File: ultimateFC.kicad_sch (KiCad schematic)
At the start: 73 parts, among them J1 USB_B_Micro, U14 TPS62824ADMQ, U32 LMR33630CQRNX, U33 STM32H735VGH6, U36 ICM-20602, U37 S25FL064L, U39 BMP280, Y1 CSTNE8M00G550000R0

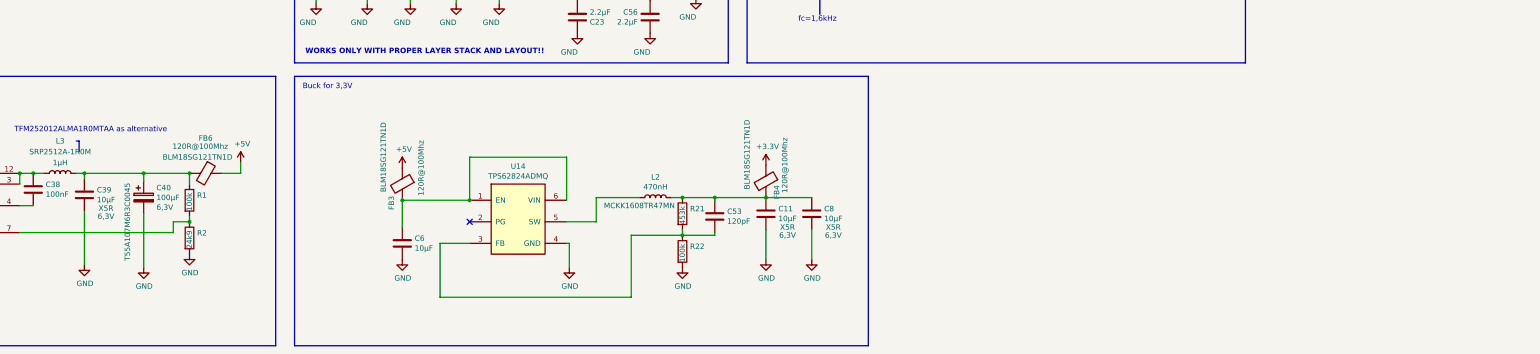
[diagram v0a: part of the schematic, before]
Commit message: add HD DCDC
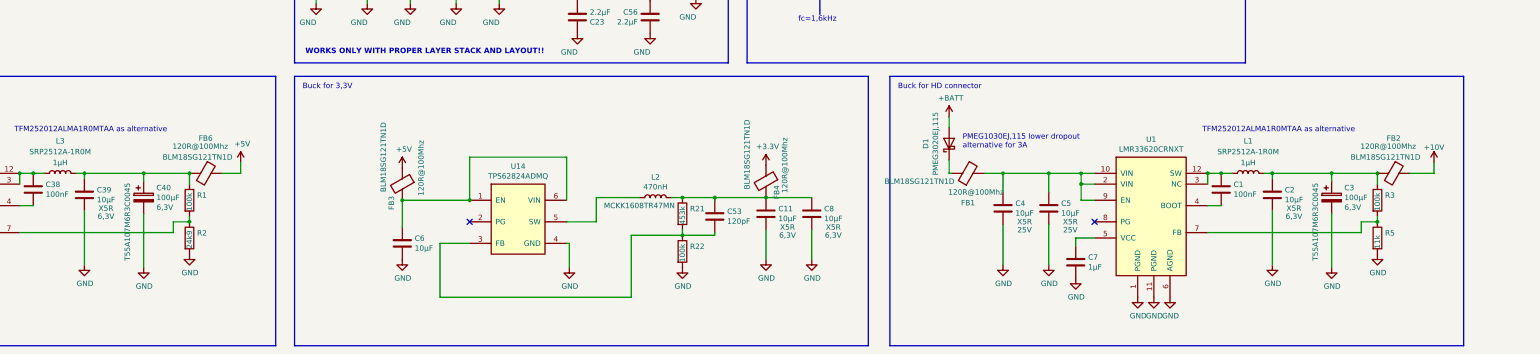
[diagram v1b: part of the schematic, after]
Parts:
- added C1: 100nF, ultimateFC:C_0201_0603Metric_mod, symbol Device:C
- added C2: 10µF, Capacitor_SMD:C_0603_1608Metric, symbol Device:C
- added C3: 100µF, Capacitor_Tantalum_SMD:CP_EIA-3216-10_Kemet-I, symbol ultimateFC-rescue:CP-Device
- added C4, C5: 10µF, Capacitor_SMD:C_1206_3216Metric, symbol Device:C
- added C7: 1µF, Capacitor_SMD:C_0402_1005Metric, symbol Device:C
- added D1: PMEG3020EJ,115, Diode_SMD:D_SOD-323, symbol Device:D_Schottky
- added FB1, FB2: 120R@100Mhz, Inductor_SMD:L_0603_1608Metric, symbol ultimateFC-rescue:Ferrite_Bead-Device
- added L1: 1µH, Inductor_SMD:L_Wuerth_MAPI-2506, symbol Device:L
- added R3: 100k, ultimateFC:R_0201_0603Metric_mod, symbol Device:R
- added R5: 11k, ultimateFC:R_0201_0603Metric_mod, symbol Device:R
- added U1: LMR33620CRNXT, ultimateFC:Texas_RNX0012B, symbol ultimateFC-rescue:LMR33630CQRNX-lib_ultimateFC
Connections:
- net +BATT: now also D1.2 (A)
- net GND: now also C2.2, C3.2, C4.2, C5.2, C7.2, R5.2, U1.1 (PGND), U1.11 (PGND), U1.6 (AGND)
- new net: C4.1, C5.1, FB1.2, U1.10 (VIN), U1.2 (VIN), U1.9 (EN)
- new net: C1.1, L1.1, U1.12 (SW), U1.3 (NC)
- new net: C1.2, U1.4 (BOOT)
- new net: D1.1 (K), FB1.1
- new net: C2.1, C3.1, FB2.2, L1.2, R3.1
- new net: R3.2, R5.1, U1.7 (FB)
- new net: C7.1, U1.5 (VCC)
- new net +10V: FB2.1
- no-connect marks 5 -> 6
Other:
- note added: "Buck for HD connector"

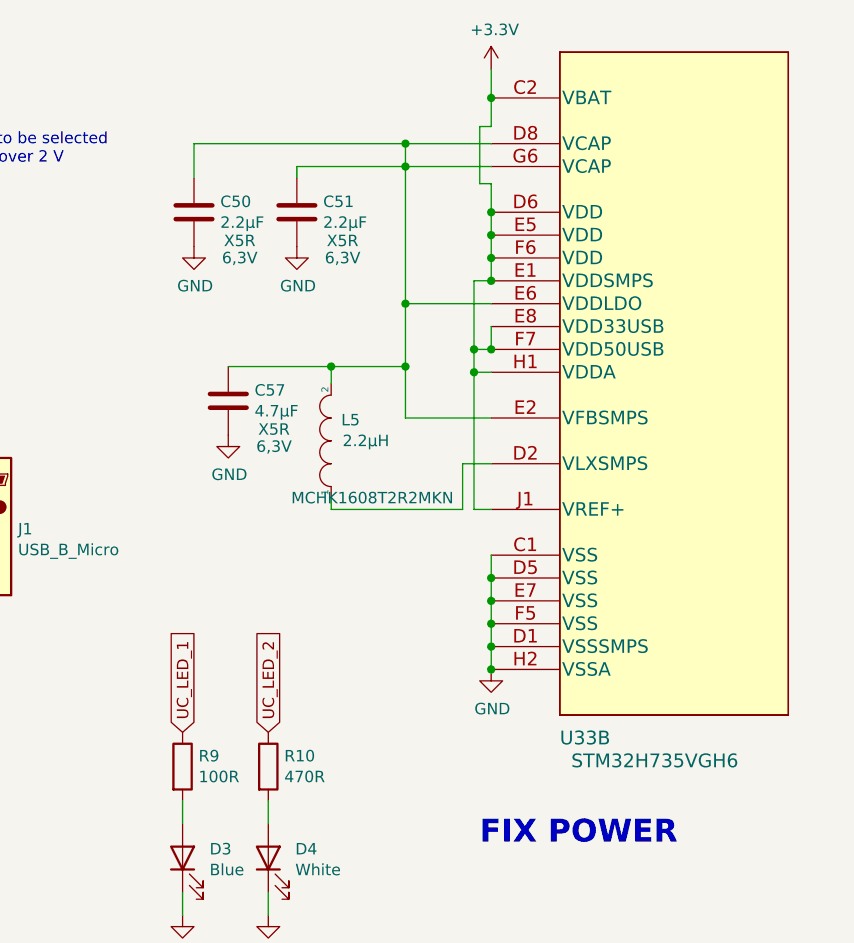
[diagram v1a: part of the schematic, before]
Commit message: update H7 Power symbol (!)
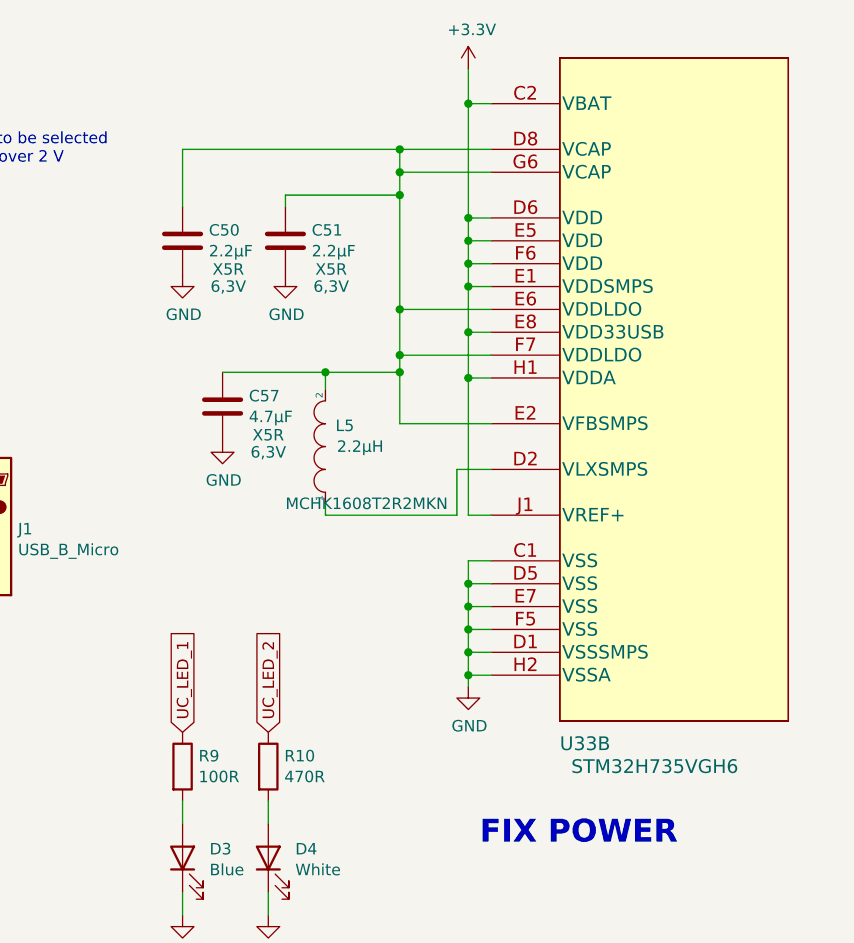
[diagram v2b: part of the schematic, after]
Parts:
- U33: footprint Package_BGA:TFBGA-100_8x8mm_Layout10x10_P0.8mm -> TFBGA100_8X8_STM
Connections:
- net +3V3: no longer U33.F7 (VDD50USB)
- net at C50.1, C51.1, C57.1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: now also U33.F7 (VDDLDO)
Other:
- moved on the sheet: C50, C51, C57, L5, U33B

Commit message: added PADs.... lots of PADs
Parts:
- removed C2: 10µF, Capacitor_SMD:C_0603_1608Metric, symbol Device:C
- removed C22, C23, C24, C25: 2.2µF, Capacitor_SMD:C_0603_1608Metric, symbol Device:C
- removed C27: 10µF, Capacitor_Tantalum_SMD:CP_EIA-3216-18_Kemet-A, symbol ultimateFC-rescue:CP-Device
- removed D1: PMEG3020EJ,115, Diode_SMD:D_SOD-323, symbol Device:D_Schottky
- added C31: 10µF, Capacitor_SMD:C_1206_3216Metric, symbol Device:C
- added C33: 100µF, Capacitor_Tantalum_SMD:CP_EIA-3528-12_Kemet-T, symbol ultimateFC-rescue:CP-Device
- added C34: 4.7µF, Capacitor_SMD:C_0402_1005Metric, symbol Device:C
- added R12, R13, R14, R15, R16, R17, R18, R19, R20, R21, R23: 100R, ultimateFC:R_0201_0603Metric_mod, symbol Device:R
- added TP1, TP10, TP100, TP101, TP102, TP103, TP104, TP105, TP106, TP107, TP108, TP109, TP11, TP110, TP12, TP13, TP14, TP15, TP16, TP17, TP18, TP19, TP2, TP22, TP23, TP24, TP25, TP26, TP27, TP29, TP3, TP30, TP31, TP32, TP33, TP34, TP35, TP36, TP37, TP38, TP39, TP4, TP40, TP41, TP42, TP43, TP44, TP45, TP46, TP47, TP48, TP49, TP5, TP50, TP51, TP52, TP53, TP54, TP55, TP56, TP57, TP58, TP59, TP6, TP60, TP61, TP62, TP63, TP64, TP65, TP66, TP67, TP68, TP69, TP7, TP70, TP71, TP72, TP73, TP74, TP75, TP76, TP77, TP78, TP79, TP8, TP80, TP81, TP82, TP83, TP84, TP85, TP86, TP87, TP88, TP89, TP9, TP90, TP91, TP92, TP93, TP94, TP95, TP96, TP97, TP98, TP99: Pad, TestPoint:TestPoint_Pad_1.5x1.5mm, symbol Connector:TestPoint_Flag
- added TP20, TP21: Pad, TestPoint:TestPoint_Pad_3.0x3.0mm, symbol Connector:TestPoint_Flag
- added U6: BMI270, Package_LGA:Bosch_LGA-14_3x2.5mm_P0.5mm, symbol Sensor_Motion:BMI160
- C10: renamed from C15; value 2.2µF -> 4.7µF; footprint ultimateFC:C_AVX_Super_Low_ESL -> Capacitor_SMD:C_0402_1005Metric
- C12: renamed from C20; value 1µF -> 4.7µF; footprint ultimateFC:C_AVX_Super_Low_ESL -> Capacitor_SMD:C_0402_1005Metric
- C13: renamed from C21; value 2.2µF -> 4.7µF; footprint ultimateFC:C_AVX_Super_Low_ESL -> Capacitor_SMD:C_0402_1005Metric
- C14: renamed from C41; value 1µF -> 4.7µF; footprint ultimateFC:C_AVX_Super_Low_ESL -> Capacitor_SMD:C_0402_1005Metric
- C15: renamed from C42; value 2.2µF -> 4.7µF; footprint ultimateFC:C_AVX_Super_Low_ESL -> Capacitor_SMD:C_0402_1005Metric
- C16: renamed from C43; value 1µF -> 4.7µF; footprint ultimateFC:C_AVX_Super_Low_ESL -> Capacitor_SMD:C_0402_1005Metric
- C17: renamed from C44; value 2.2µF -> 4.7µF; footprint ultimateFC:C_AVX_Super_Low_ESL -> Capacitor_SMD:C_0402_1005Metric
- C29: renamed from C7; footprint Capacitor_SMD:C_0402_1005Metric -> ultimateFC:C_0201_0603Metric_mod
- C3: renamed from C37; footprint Capacitor_SMD:C_0402_1005Metric -> ultimateFC:C_0201_0603Metric_mod
- C32: renamed from C3; footprint Capacitor_Tantalum_SMD:CP_EIA-3216-10_Kemet-I -> Capacitor_Tantalum_SMD:CP_EIA-3528-12_Kemet-T; Mfr.No: T55A107M6R3C0045 -> T599B107M2R5ATE055; Spannung 6,3V -> 10V
- C35: renamed from C52; value 2.2µF -> 4.7µF
- C36: renamed from C50; value 2.2µF -> 4.7µF
- C38: renamed from C51; value 2.2µF -> 4.7µF
- C9: renamed from C14; value 1µF -> 4.7µF; footprint ultimateFC:C_AVX_Super_Low_ESL -> Capacitor_SMD:C_0402_1005Metric
- H1: renamed from H3; footprint MountingHole:MountingHole_3.2mm_M3 -> MountingHole:MountingHole_3.2mm_M3_DIN965_Pad; symbol Mechanical:MountingHole -> Mechanical:MountingHole_Pad
- H2: renamed from H1; footprint MountingHole:MountingHole_3.2mm_M3 -> MountingHole:MountingHole_3.2mm_M3_DIN965_Pad; symbol Mechanical:MountingHole -> Mechanical:MountingHole_Pad
- H3: renamed from H2; footprint MountingHole:MountingHole_3.2mm_M3 -> MountingHole:MountingHole_3.2mm_M3_DIN965_Pad; symbol Mechanical:MountingHole -> Mechanical:MountingHole_Pad
- H4: footprint MountingHole:MountingHole_3.2mm_M3 -> MountingHole:MountingHole_3.2mm_M3_DIN965_Pad; symbol Mechanical:MountingHole -> Mechanical:MountingHole_Pad
- renumbered C35 to C1, C6 to C11, C55 to C18, C45 to C19, C36 to C2, C56 to C20, C46 to C21, C26 to C22, C53 to C23, C11 to C24, C28 to C25, C8 to C26, C4 to C27, C5 to C28, C1 to C30, C57 to C37, C38 to C4, C39 to C5, C40 to C6, C12 to C7, C13 to C8, D101 to D1, D3 to D2, D4 to D3, D2 to D4, FB5 to FB1, FB6 to FB2, FB1 to FB5, FB2 to FB6, L3 to L1, L1 to L3, L5 to L4, R5 to R10, R30 to R11, R4 to R22, R9 to R24, R10 to R25, R7 to R26, R8 to R27, R21 to R3, R22 to R4, R47 to R5, R48 to R6, R36 to R7, R37 to R8, R3 to R9, TP29 to TP28, U32 to U1, U14 to U2, U1 to U3, U37 to U4, U39 to U5, U33 to U7, U36 to U8
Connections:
- net +10V: now also C33.1, C34.1, TP14.1, TP15.1
- net +3V3: now also TP3.1, TP4.1, TP66.1, U6.5 (VDDIO), U6.8 (VDD)
- net +5V: now also TP1.1, TP2.1
- net +BATT: now also FB5.1, TP20.1
- net CS_FLASH: now also TP95.1; no longer U4.1 (~{CS})
- net CS_GYRO: now also TP90.1; no longer U8.5 (~{CS})
- net CS_OSD: now also TP45.1
- net ESC_1_TX: now also TP110.1
- net ESC_2_TX: now also TP109.1
- net ESC_3_TX: now also TP61.1
- net ESC_4_TX: now also TP62.1
- net GND: now also H1.1, H2.1, H3.1, H4.1, C31.2, C33.2, C34.2, TP16.1, TP17.1, TP21.1, TP5.1, TP6.1, TP65.1, TP7.1, TP8.1, U6.6 (GNDIO), U6.7 (GND)
- net I2C_SCL: now also TP43.1; no longer R8.2, U5.4 (SCK)
- net I2C_SDA: now also TP44.1; no longer R7.2, U5.3 (SDI)
- net MISO_FLASH: now also TP96.1; no longer U4.2 (DO(IO1))
- net MISO_GYRO: now also TP82.1; no longer U8.4 (SAO/SD0)
- net MISO_OSD: now also TP47.1
- net MOSI_FLASH: now also TP97.1; no longer U4.5 (DI(IO0))
- net MOSI_GYRO: now also TP83.1; no longer U8.3 (SDA/SDI)
- net MOSI_OSD: now also TP48.1
- net MOTOR1: now also TP77.1
- net MOTOR2: now also TP80.1
- net MOTOR3: now also TP79.1
- net MOTOR4: now also TP78.1
- net MP_PIN1: now also TP33.1
- net MP_PIN2: now also TP106.1
- net MP_PIN3: now also TP105.1
- net MP_PIN4: now also TP34.1
- net MP_PIN5: now also TP39.1
- net MP_PIN6: now also TP40.1
- net SCLK_FLASH: now also TP93.1; no longer U4.6 (CLK)
- net SCLK_GYRO: now also TP81.1; no longer U8.2 (SCL/SPC)
- net SCLK_OSD: now also TP46.1
- net UART2_RX: now also TP55.1
- net UART2_TX: now also TP54.1
- net UART3_RX: now also TP58.1
- net UART3_TX: now also TP57.1
- net UART4_RX: now also TP104.1
- net UART4_TX: now also TP103.1
- net UART7_RX: now also TP98.1
- net UART7_TX: now also TP99.1
- net UART8_RX: now also TP91.1
- net UART8_TX: now also TP92.1
- net UART9_RX: now also TP64.1
- net UART9_TX: now also TP63.1
- net UC_LED_1: now also TP51.1; no longer R24.1
- net UC_LED_2: now also TP59.1; no longer R25.1
- net curr_sig: now also TP108.1
- net vol_sig: now also TP76.1; no longer C25.1, R5.2, R6.1
- net at R22.2, U7.F2 (NRST): now also TP67.1
- net at U7.A4 (PB8): now also TP41.1
- net at U7.A6 (PB5): now also TP38.1
- net at U7.A8 (PD3): now also TP52.1
- net at U7.B1 (PC14-OSC32_IN): now also TP85.1
- net at U7.B2 (PC15-OSC32_OUT): now also TP102.1
- net at U7.B3 (PE3): now also TP94.1
- net at U7.B6 (PB3): now also TP36.1
- net at U7.B7 (PD4): now also TP53.1
- net at U7.B8 (PD1): now also TP50.1
- net at U7.C5 (PB4): now also TP37.1
- net at U7.C6 (PD7): now also TP56.1
- net at U7.C7 (PD0): now also TP49.1
- net SWDCLK: now reaches U7.C9 (PA14)
- net SWDCLK: now also TP89.1
- net at U7.E10 (PA10): now also TP87.1
- net at U7.E3 (PB9): now also TP42.1
- net at U7.E4 (PC13): now also TP84.1
- net at U7.F1 (PC1): now also TP72.1
- net at U7.F10 (PA8): now also TP86.1
- net at U7.F3 (PC0): now also TP71.1
- net at U7.F4 (PC2_C): now also TP73.1
- net at U7.G4 (PC3_C): now also TP74.1
- net at U7.H4 (PC4): now also TP75.1
- net at U7.H6 (PE10): now also TP101.1
- net at U7.H7 (PD11): now also TP60.1
- net at U7.J5 (PB2): now also TP35.1
- net at U7.K1 (PA4): now also TP107.1
- net at U7.K6 (PE9): now also TP100.1
- net at C32.1, FB6.2, L3.2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: now also C31.1
- net INT_GYRO: no longer names the net of U8.6 (INT)
- net INT_GYRO: now also R23.1; no longer U7.C10 (PA13)
- new net: R7.2, TP11.1, U5.3 (SDI)
- new net: R8.2, TP10.1, U5.4 (SCK)
- new net: C25.1, R5.2, R6.1, TP9.1
- new net: R20.2, U8.2 (SCL/SPC)
- new net: R19.2, U8.3 (SDA/SDI)
- new net: R18.2, U8.4 (SAO/SD0)
- new net: R21.2, U8.5 (~{CS})
- new net: TP13.1, U4.1 (~{CS})
- new net: TP19.1, U4.2 (DO(IO1))
- new net: TP18.1, U4.5 (DI(IO0))
- new net: TP12.1, U4.6 (CLK)
- new net: R24.1, TP69.1
- new net: R25.1, TP70.1
- new net: R15.1, TP25.1
- new net: R15.2, U6.12 (CSB)
- new net: R17.1, TP27.1
- new net: R17.2, U6.9 (INT2)
- new net: R19.1, TP30.1
- new net: R21.1, TP32.1
- new net: R23.2, TP68.1
- new net: R13.1, TP23.1
- new net: R16.1, TP26.1
- new net: R12.1, TP22.1
- new net: R18.1, TP29.1
- new net: R13.2, U6.14 (SDx)
- new net: R12.2, U6.1 (SDO)
- new net: R14.2, U6.13 (SCx)
- new net: R16.2, U6.4 (INT1)
- new net: R20.1, TP31.1
- new net: R14.1, TP24.1
- new net SWDIO: TP88.1, U7.C10 (PA13)
- no-connect marks 6 -> 10
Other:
- note added: "DPS310 Pin compatible?"
- note removed: "UPDATE BARO!!!"
- note removed: "WORKS ONLY WITH PROPER LAYER STACK AND LAYOUT!!"
- moved on the sheet: C35, D2, D3, R24, R25, R7, R8, U5, U8

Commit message: schematic and layout update
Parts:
- removed U5: BMP280, Package_LGA:Bosch_LGA-8_2x2.5mm_P0.65mm_ClockwisePinNumbering, symbol Sensor_Pressure:BMP280
- added R28: 14k, Resistor_SMD:R_0402_1005Metric, symbol Device:R
- added TP111: bridge, ultimateFC:solderbridge_tiny, symbol ultimateFC-rescue:Jumper-Device
- added U5: DPS310, Package_LGA:Bosch_LGA-8_2x2.5mm_P0.65mm_ClockwisePinNumbering, symbol ultimateFC-rescue:DPS310
- C23, C25, C29, C3, C30, C4: footprint ultimateFC:C_0201_0603Metric_mod -> Capacitor_SMD:C_0402_1005Metric
- D2, D3: footprint LED_SMD:LED_0201_0603Metric -> LED_SMD:LED_0402_1005Metric
- R1, R10, R11, R12, R13, R14, R15, R16, R17, R18, R19, R2, R20, R21, R22, R23, R24, R25, R26, R27, R3, R4, R6, R7, R8, R9: footprint ultimateFC:R_0201_0603Metric_mod -> Resistor_SMD:R_0402_1005Metric
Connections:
- net +3V3: now also U5.2 (CSB), U5.6 (VDDIO), U5.8 (VDD)
- net GND: now also R28.2, TP111.2, U5.1 (GND), U5.5 (SDO), U5.7 (GND); no longer R10.2
- net SCL_DPS: now reaches R7.2, TP11.1
- net SCL_DPS: now also U5.3 (SDI)
- net SCK_DPS: now reaches R8.2, TP10.1
- net SCK_DPS: now also U5.4 (SCK)
- net CS_FLASH_IC: now reaches TP13.1, U4.1 (~{CS})
- net MISO_FLASH_IC: now reaches TP19.1, U4.2 (DO(IO1))
- net MOSI_FLASH_IC: now reaches TP18.1, U4.5 (DI(IO0))
- net SCK_FLASH_IC: now reaches TP12.1, U4.6 (CLK)
- net USB_VBUS_sense: now reaches R26.2, R27.1, U7.E9 (PA9)
- net A_LED_BL: now reaches R24.1, TP69.1
- net A_LED_WT: now reaches R25.1, TP70.1
- net CS_270: now reaches R15.1, TP25.1
- net INT2_270: now reaches R17.1, TP27.1
- net MOSI_20602: now reaches R19.1, TP30.1
- net CS_20602: now reaches R21.1, TP32.1
- net INT_20602: now reaches R23.2, TP68.1
- net MOSI_270: now reaches R13.1, TP23.1
- net INT1_270: now reaches R16.1, TP26.1
- net MISO_270: now reaches R12.1, TP22.1
- net MISO_20602: now reaches R18.1, TP29.1
- net SCK_20602: now reaches R20.1, TP31.1
- net SCK_270: now reaches R14.1, TP24.1
- new net: R10.2, R28.1, TP111.1
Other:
- note removed: "DPS310 Pin compatible?"
- note removed: "MISO"
- note removed: "MOSI"
- note removed: "SCK"
- moved on the sheet: C33, C34, C35, D2, D3, FB6, R10, R12, R13, R14, R15, R16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

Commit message: more layout
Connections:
- net UC_LED_2: no longer TP59.1, U7.J10 (PD10)
- net IMU_INT1B: now reaches TP60.1, U7.H7 (PD11)
- new net IMU_INT1A: TP59.1, U7.J10 (PD10)
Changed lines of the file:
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@@
+    )
+  )
+  (global_label "IMU_INT1A" (shape input) (at 538.48 127 180) (fields_autoplaced)
+    (effects (font (size 1.27 1.27)) (justify right))
+    (property "Intersheet References" "${INTERSHEET_REFS}" (id 0) (at 526.6006 126.9206 0)
+      (effects (font (size 1.27 1.27)) (justify right) hide)
     )
   )
@@
     )
   )
-  (global_label "UC_LED_2" (shape input) (at 542.29 127 180) (fields_autoplaced)
+  (global_label "UC_LED_2" (shape input) (at 490.22 115.57 180) (fields_autoplaced)
     (effects (font (size 1.27 1.27)) (justify right))
-    (property "Intersheet References" "${INTERSHEET_REFS}" (id 0) (at 0 0 0)
+    (property "Intersheet References" "${INTERSHEET_REFS}" (id 0) (at -52.07 -11.43 0)
       (effects (font (size 1.27 1.27)) hide)
     )
@@
     )
   )
+  (global_label "IMU_INT1B" (shape input) (at 538.48 129.54 180) (fields_autoplaced)
+    (effects (font (size 1.27 1.27)) (justify right))
+    (property "Intersheet References" "${INTERSHEET_REFS}" (id 0) (at 526.4191 129.4606 0)
+      (effects (font (size 1.27 1.27)) (justify right) hide)
+    )
+  )

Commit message: layout update
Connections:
- net NRST: now reaches R22.2, TP67.1, U7.F2 (NRST)
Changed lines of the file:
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@@
+    (effects (font (size 1.27 1.27)) (justify left bottom))
+  )
+  (label "NRST" (at 535.94 53.34 0)
     (effects (font (size 1.27 1.27)) (justify left bottom))
   )

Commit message: update layout
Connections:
- net UC_LED_1: now also TP87.1, U7.E10 (PA10); no longer TP51.1, U7.A9 (PD2)
- net UC_LED_2: now also TP86.1, U7.F10 (PA8)
- new net: TP51.1, U7.A9 (PD2)
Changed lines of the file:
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@@
     )
   )
-  (global_label "UC_LED_2" (shape input) (at 490.22 115.57 180) (fields_autoplaced)
-    (effects (font (size 1.27 1.27)) (justify right))
-    (property "Intersheet References" "${INTERSHEET_REFS}" (id 0) (at -52.07 -11.43 0)
+  (global_label "UC_LED_2" (shape input) (at 618.49 69.85 0) (fields_autoplaced)
+    (effects (font (size 1.27 1.27)) (justify left))
+    (property "Intersheet References" "${INTERSHEET_REFS}" (id 0) (at 1160.78 196.85 0)
       (effects (font (size 1.27 1.27)) hide)
     )
@@
     )
   )
-  (global_label "UC_LED_1" (shape input) (at 538.48 106.68 180) (fields_autoplaced)
-    (effects (font (size 1.27 1.27)) (justify right))
-    (property "Intersheet References" "${INTERSHEET_REFS}" (id 0) (at -3.81 0 0)
+  (global_label "UC_LED_1" (shape input) (at 618.49 74.93 0) (fields_autoplaced)
+    (effects (font (size 1.27 1.27)) (justify left))
+    (property "Intersheet References" "${INTERSHEET_REFS}" (id 0) (at 1160.78 181.61 0)
       (effects (font (size 1.27 1.27)) hide)
     )

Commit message: add WS2812, update layout
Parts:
- removed TP28: bridge, ultimateFC:solderbridge_tiny, symbol ultimateFC-rescue:Jumper-Device
- added D5: WS2812B, LED_SMD:LED_WS2812B_PLCC4_5.0x5.0mm_P3.2mm, symbol LED:WS2812B
- added D6: SBR1A30T5-7, Diode_SMD:D_SOD-523, symbol Device:D_Schottky
- added SW1: SW_Push, Button_Switch_SMD:SW_Push_1P1T_NO_CK_KMR2, symbol Switch:SW_Push
- added TP112, TP113, TP114, TP115, TP116, TP28: Pad, TestPoint:TestPoint_Pad_1.5x1.5mm, symbol Connector:TestPoint_Flag
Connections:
- net +3V3: now also SW1.2
- net +5V: now also D6.2 (A), TP113.1, TP116.1, TP28.1
- net +BATT: now also TP112.1
- net GND: now also D5.3 (VSS)
- net at R11.1, U7.A5 (BOOT0): now also SW1.1
- new net: D5.1 (VDD), D6.1 (K)
- new net WS_IN: D5.4 (DIN), TP114.1
- new net WS_OUT: D5.2 (DOUT), TP115.1
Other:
- moved on the sheet: TP1, TP14, TP15, TP16, TP17, TP2
